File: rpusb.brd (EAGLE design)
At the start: 75 x 53 mm, 105 parts, among them IC1 M24C02-FMH6TG, IC2 RP2040, IC3 RP2040, IC4 16MB_Flash, IC5 16MB_Flash, IC6 AP7362-33SP-13, J2 Micro-B, J3 Micro-B

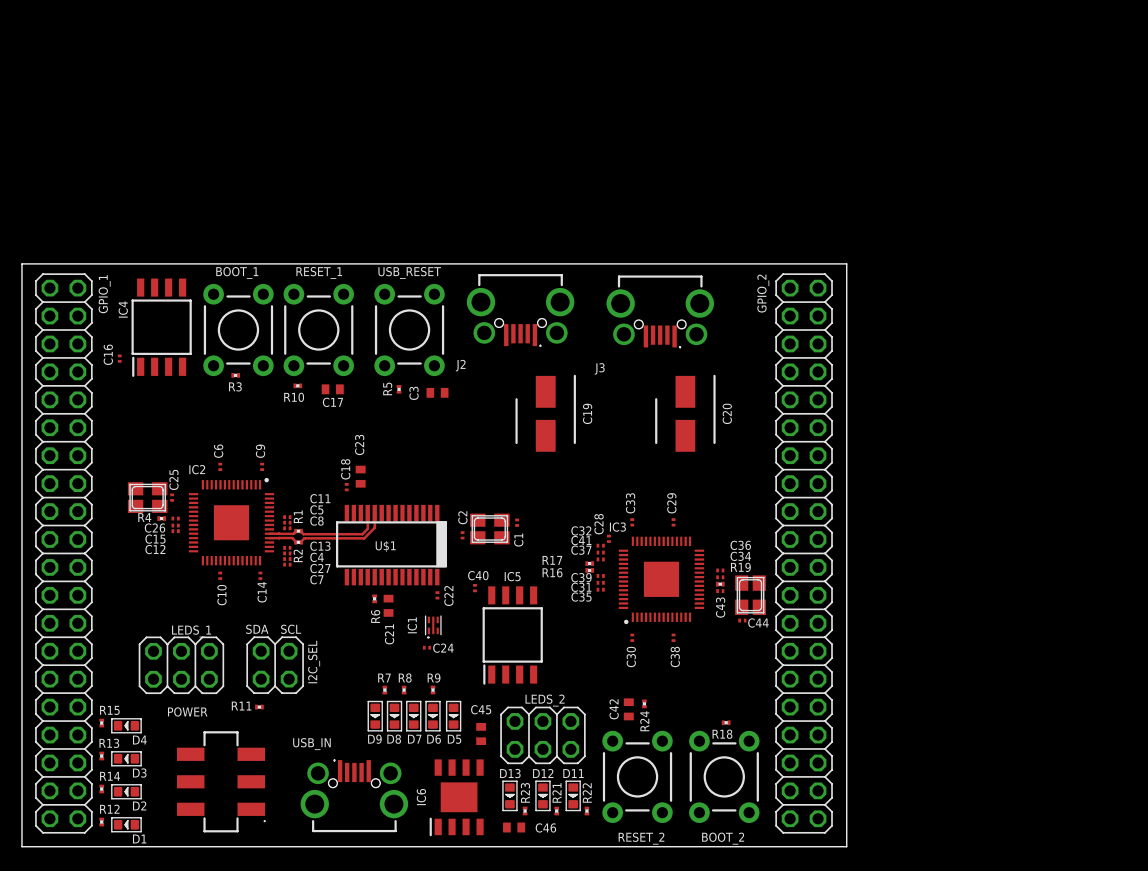
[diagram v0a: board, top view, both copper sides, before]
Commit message: First stab at routing the board - set up for JCLPCB
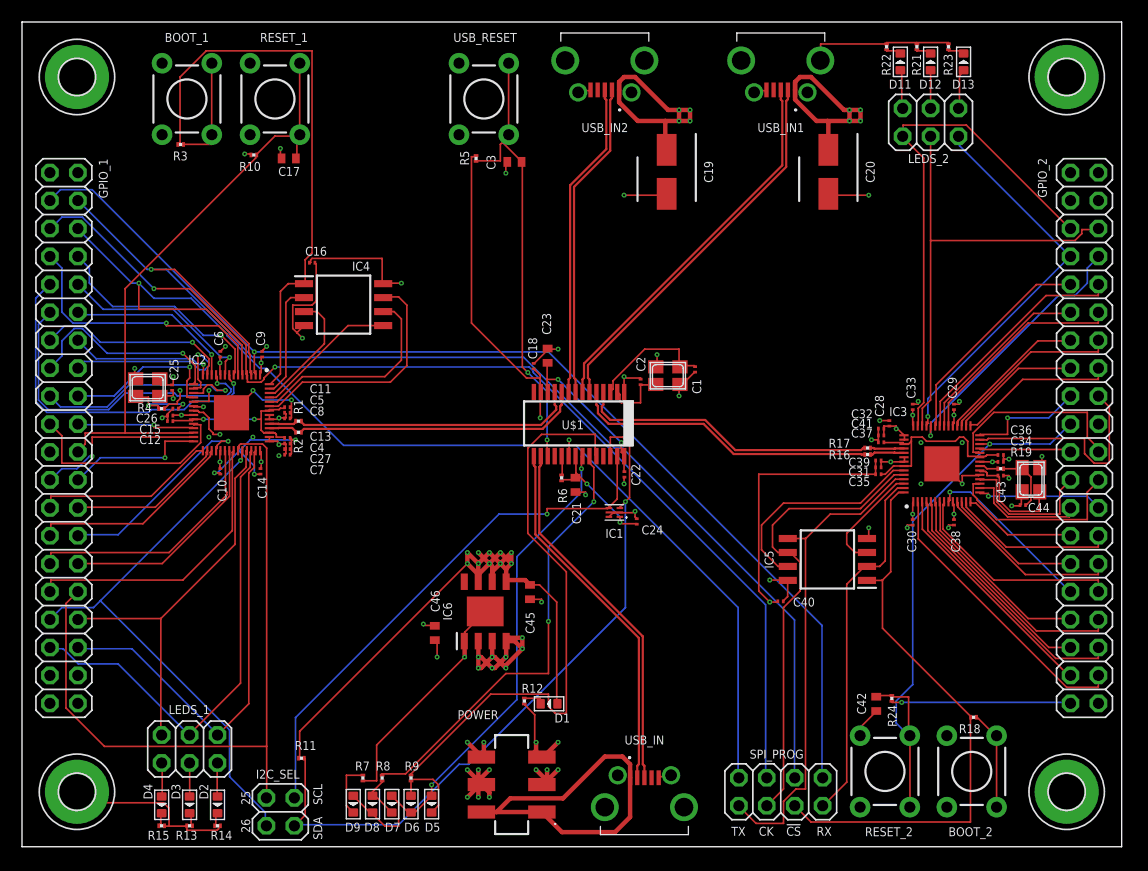
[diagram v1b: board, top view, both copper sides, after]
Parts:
- removed J2, J3: Micro-B, samacsys:MCRBSRASMTCS14TR
- added H1, H2, H3, H4: MOUNT-PAD-ROUND3.2, holes:3,2-PAD
- added SPI_PROG: (no value), pinhead:2X04
- added USB_IN1, USB_IN2: U254-051T-4BHJ25-S2S, samacsys:U254051T4BHJ25S2S
- Q1, Q2, Q3: value (none) -> 12MHz
- USB_IN: value Micro-B -> U254-051T-4BHJ25-S2S; device samacsys:MCRBSRASMTCS14TR -> samacsys:U254051T4BHJ25S2S
- moved R23 79.5 mm to (84.2, 72.8), turned to 90 degrees
- moved D13 78.5 mm to (85.6, 71.4), turned to 90 degrees
- moved R21 76.8 mm to (81.4, 72.8), turned to 90 degrees
- moved D12 75.5 mm to (82.6, 71.4), turned to 90 degrees
- moved R22 74.7 mm to (78.6, 72.8), turned to 90 degrees
- moved D11 73.1 mm to (79.9, 71.4), turned to 90 degrees
- moved LEDS_2 66.0 mm to (82.6, 65.9), turned to 0 degrees
- moved D1 40.0 mm to (47.9, 13.0)
- moved R12 40.0 mm to (45.7, 13.2)
- moved IC5 29.4 mm to (73.2, 26.1), turned to 180 degrees
- moved C40 27.8 mm to (69.0, 22.3), turned to 180 degrees
- moved C32 27.6 mm to (78.1, 38.0)
- moved C37 27.6 mm to (78.1, 36.8)
- moved C41 27.6 mm to (78.1, 37.4)
- moved IC3 27.6 mm to (83.7, 34.8)
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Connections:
- net !QSPI2_SS!: now also SPI_PROG.4
- net +5V: now also USB_IN1.1, USB_IN2.1; no longer J2.1, J3.1
- net GND: now also H1.B3,2, H2.B3,2, H3.B3,2, H4.B3,2, IC6.1, USB_IN1.5, USB_IN1.MH1, USB_IN1.MH2, USB_IN1.MH3, USB_IN1.MH4, USB_IN2.5, USB_IN2.MH1, USB_IN2.MH2, USB_IN2.MH3, USB_IN2.MH4; no longer J2.5, J2.MH1, J2.MH2, J2.MH3, J2.MH4, J3.5, J3.MH1, J3.MH2, J3.MH3, J3.MH4
- net GPIO0: now also SPI_PROG.1
- net GPIO1: now also SPI_PROG.3
- net GPIO2: now also SPI_PROG.5
- net GPIO3: now also SPI_PROG.7
- net N$19: now also D6.-, D7.+
- net QSPI2_CLK: now also SPI_PROG.6
- net QSPI2_SD0: now also SPI_PROG.8
- net QSPI2_SD1: now also SPI_PROG.2
- net USB_D2_N: now also USB_IN2.2; no longer J2.2
- net USB_D2_P: now also USB_IN2.3; no longer J2.3
- net USB_D3_N: now also USB_IN1.2; no longer J3.2
- net USB_D3_P: now also USB_IN1.3; no longer J3.3
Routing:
- net GND: track 0.00 -> 180.9 mm, vias 0 -> 48
- net +3V3_RP: track 0.00 -> 123.3 mm, vias 0 -> 29
- net GPIO1: track 0.00 -> 110.0 mm, vias 0 -> 1
- net GPIO3: track 0.00 -> 105.7 mm, vias 0 -> 1
- net GPIO0: track 0.00 -> 103.1 mm, vias 0 -> 1
- net GPIO2: track 0.00 -> 99.1 mm, vias 0 -> 2
- net +5V: track 0.00 -> 77.9 mm, vias 0 -> 27
- net GPIO25: track 0.00 -> 65.8 mm
- net RP_SDA: track 0.00 -> 64.5 mm, vias 0 -> 1
- net !RESET_RP1!: track 0.00 -> 55.8 mm
- net N$20: track 0.00 -> 52.9 mm
- net !RESET_RP2!: track 0.00 -> 52.8 mm, vias 0 -> 1
- net !QSPI2_SS!: track 0.00 -> 52.4 mm
- net !QSPI_SS!: track 0.00 -> 52.1 mm
- net GPIO26: track 0.00 -> 51.0 mm, vias 0 -> 1
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- added copper zone on layer 14, net +3V3_RP
- added copper zone on layer 15, net +5V
- added copper zone on layer 2, net GND
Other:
- board size 75 x 53 mm -> 100 x 75 mm
- board text added: "!CS!"
- board text added: "25"
- board text added: "26"
- board text added: "CK"
- board text added: "RX"
- board text added: "TX"

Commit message: Better routing
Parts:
- moved R3 11.0 mm to (25.4, 63.9)
- moved BOOT_1 11.0 mm to (26.0, 68.0)
- moved R4 6.80 mm to (19.5, 39.8)
- moved C12 6.02 mm to (19.5, 38.2)
- moved C15 6.02 mm to (19.5, 38.7)
- moved C10 6.00 mm to (24.0, 34.1)
- moved C11 6.00 mm to (30.1, 40.0)
- moved C13 6.00 mm to (30.1, 37.2)
- moved C14 6.00 mm to (27.7, 34.1)
- moved C17 6.00 mm to (18.3, 62.6)
- moved C25 6.00 mm to (19.7, 41.8)
- moved C27 6.00 mm to (30.1, 36.2)
- moved C4 6.00 mm to (30.1, 36.7)
- moved C5 6.00 mm to (30.1, 39.5)
- moved C6 6.00 mm to (24.0, 44.8)
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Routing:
- net GPIO6: track 32.2 -> 58.5 mm
- net !QSPI_SS!: track 52.1 -> 26.1 mm, vias 0 -> 2
- net SWDIO2: track 8.49 -> 26.8 mm
- net N$20: track 52.9 -> 36.0 mm, vias 0 -> 2
- net GPIO26: track 51.0 -> 64.4 mm
- net GPIO2_5: track 17.8 -> 30.3 mm, vias 0 -> 1
- net SWDIO: track 10.8 -> 23.3 mm
- net GPIO2_23: track 17.0 -> 28.5 mm, vias 0 -> 1
- net GPIO20: track 18.7 -> 30.0 mm, vias 0 -> 1
- net N$7: track 12.2 -> 1.88 mm, vias 2 -> 0
- net !RESET_RP2!: track 52.8 -> 63.0 mm
- net GPIO1: track 110.0 -> 100.1 mm
- net GPIO3: track 105.7 -> 96.0 mm
- net GPIO2: track 99.1 -> 89.7 mm, vias 2 -> 1
- net GPIO2_20: track 16.5 -> 25.7 mm, vias 0 -> 1
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- added copper zone on layer 1, net GND

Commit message: Ready to order from NextPCB
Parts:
- added TP_3V3, TP_5V, TP_GND, TP_VBUS: S1751-46R, samacsys:S175146R
- moved C2 4.00 mm to (60.3, 42.2)
- moved C21 4.00 mm to (54.3, 32.8)
- moved C22 4.00 mm to (58.8, 33.8)
- moved C23 4.00 mm to (51.8, 44.6)
- moved IC1 4.00 mm to (57.9, 30.3)
- moved Q2 4.00 mm to (62.7, 42.8)
- moved U$1 4.00 mm to (54.7, 38.4)
- moved C1 4.00 mm to (65.2, 43.3)
- moved C18 4.00 mm to (50.5, 43.6)
- moved C24 4.00 mm to (59.9, 29.5)
- moved R6 4.00 mm to (53.1, 33.5)
- moved C46 1.82 mm to (38.0, 17.7)
- moved USB_IN2 0.70 mm to (53.7, 69.4)
- moved C19 0.70 mm to (59.3, 61.3)
- moved D11 0.70 mm to (80.6, 71.3)
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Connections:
- net +3V3_RP: now also TP_3V3.1
- net +5V: now also TP_5V.1
- net GND: now also GPIO_1.37, GPIO_1.38, TP_GND.1
- net VBUS: now also TP_VBUS.1
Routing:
- net +5V: track 77.9 -> 305.5 mm, vias 27 -> 8
- net +3V3_RP: track 124.4 -> 336.1 mm, vias 28 -> 32
- net GPIO0: track 108.5 -> 151.4 mm, vias 1 -> 2
- net GND: track 187.9 -> 225.8 mm, vias 45 -> 72
- net VBUS: track 34.2 -> 71.7 mm, vias 0 -> 2
- net GPIO6: track 58.5 -> 28.3 mm
- net GPIO2_19: track 14.4 -> 29.3 mm
- net GPIO24: track 27.7 -> 40.0 mm, vias 0 -> 1
- net !RESET_RP2!: track 63.0 -> 74.3 mm, vias 1 -> 0
- net GPIO2_5: track 30.3 -> 19.5 mm
- net SWDCLK2: track 13.5 -> 23.7 mm, vias 0 -> 1
- net GPIO2_23: track 28.5 -> 19.2 mm, vias 1 -> 0
- net GPIO2_15: track 21.4 -> 12.6 mm
- net GPIO2: track 89.7 -> 98.3 mm, vias 1 -> 3
- net GPIO3: track 96.0 -> 88.7 mm, vias 1 -> 3
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- removed copper zone on layer 14, net +3V3_RP
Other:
- board text added: "!RST!"
- board text added: "0"
- board text added: "1"
- board text added: "10"
- board text added: "11"
- board text added: "12"
- board text added: "13"
- board text added: "14"
- board text added: "15"
- board text added: "16"
- board text added: "17"
- board text added: "18"
- board text added: "19"
- board text added: "2"
- board text added: "20"
- board text added: "21"
- board text added: "22"
- board text added: "23"
- board text added: "24"
- board text added: "27"
- board text added: "28"
- board text added: "29"
- board text added: "3"
- board text added: "3v3"
- board text added: "4"
- board text added: "5"
- board text added: "6"
- board text added: "7"
- board text added: "8"
- board text added: "9"
- board text added: "Clk"
- board text added: "Gnd"
- board text added: "IO"
